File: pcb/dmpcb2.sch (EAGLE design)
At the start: 75 parts, among them IC1 7805DT, IC2 L293D, IC4 LM358D, IC5 LM358D, J7 SJ-3523-SMT-TR, Q1 IRF530, Q2 IRF530

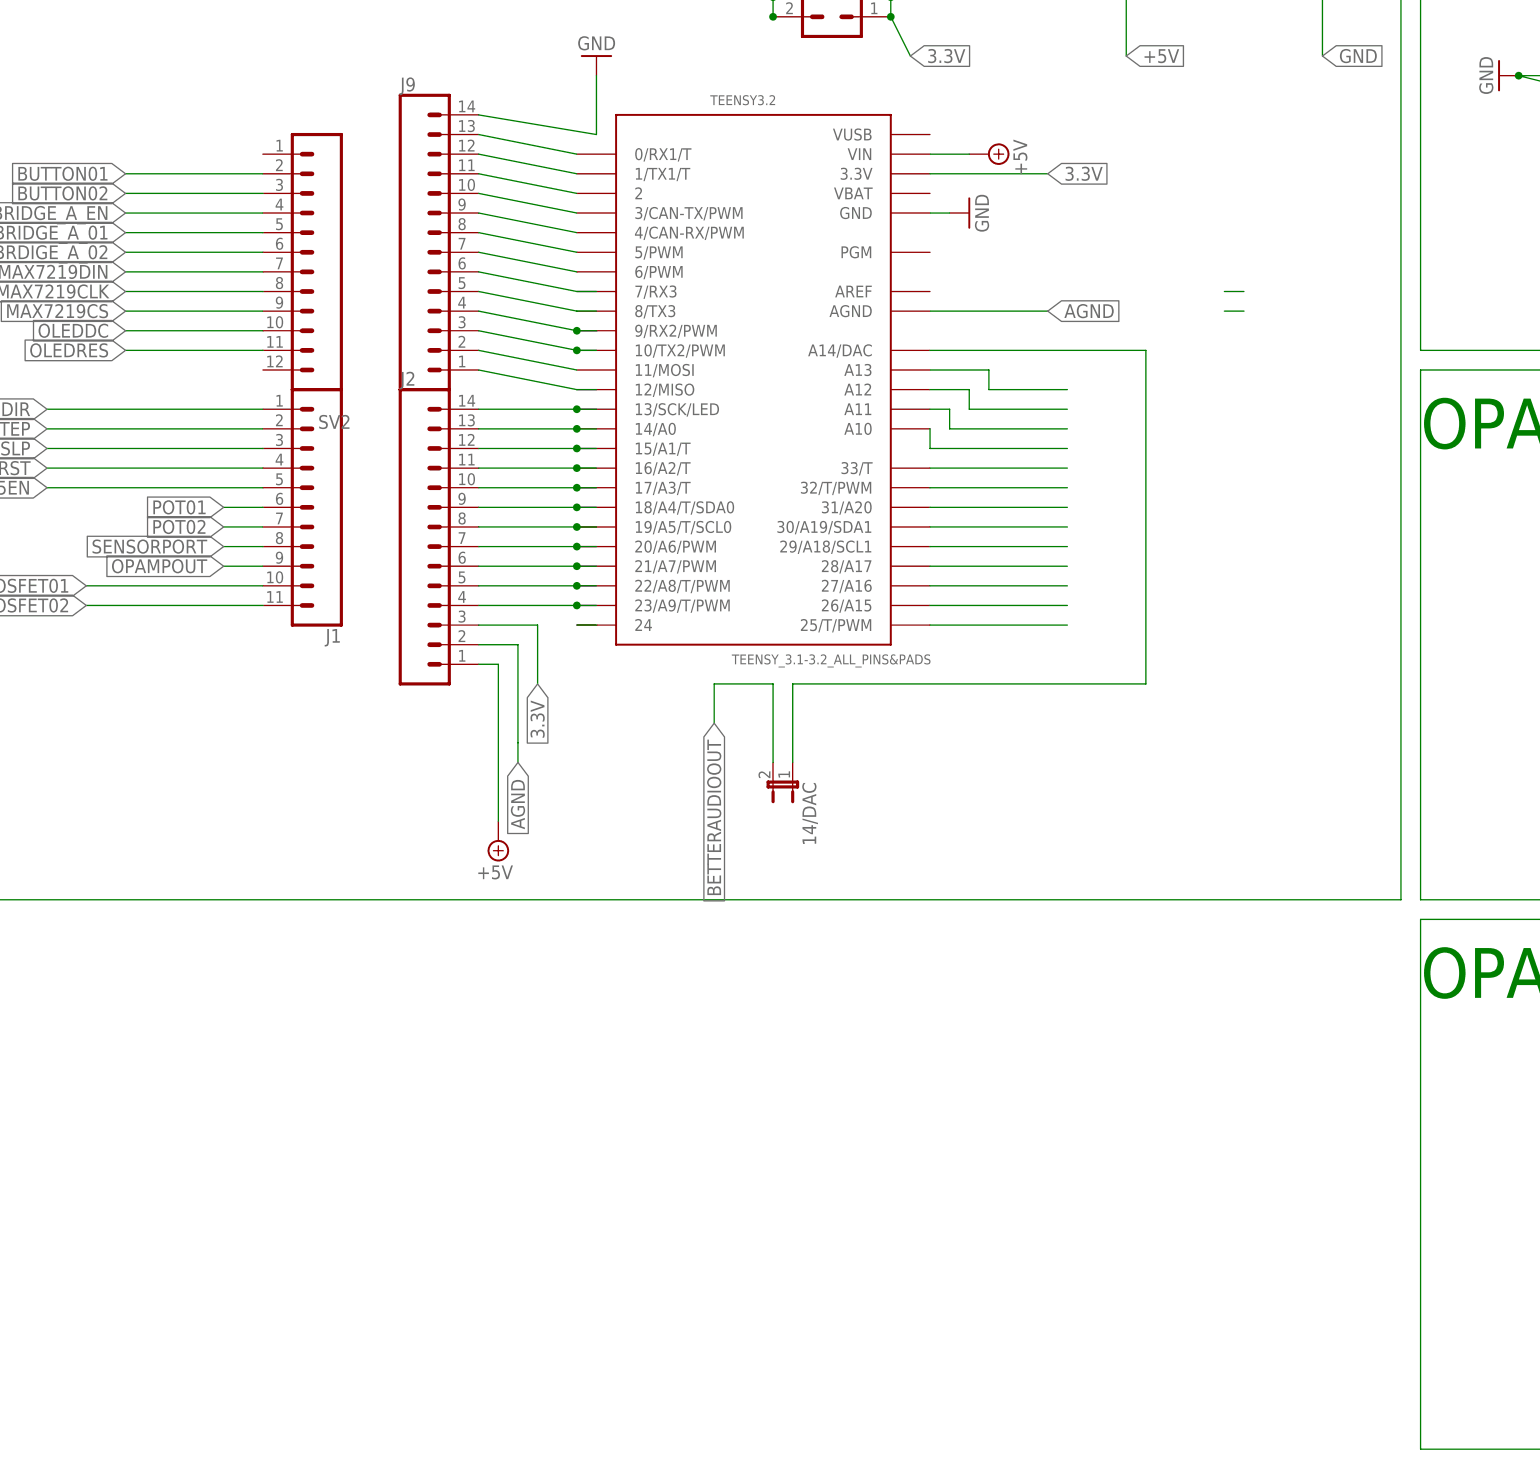
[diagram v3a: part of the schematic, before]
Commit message: added user leds and labeling for opamp
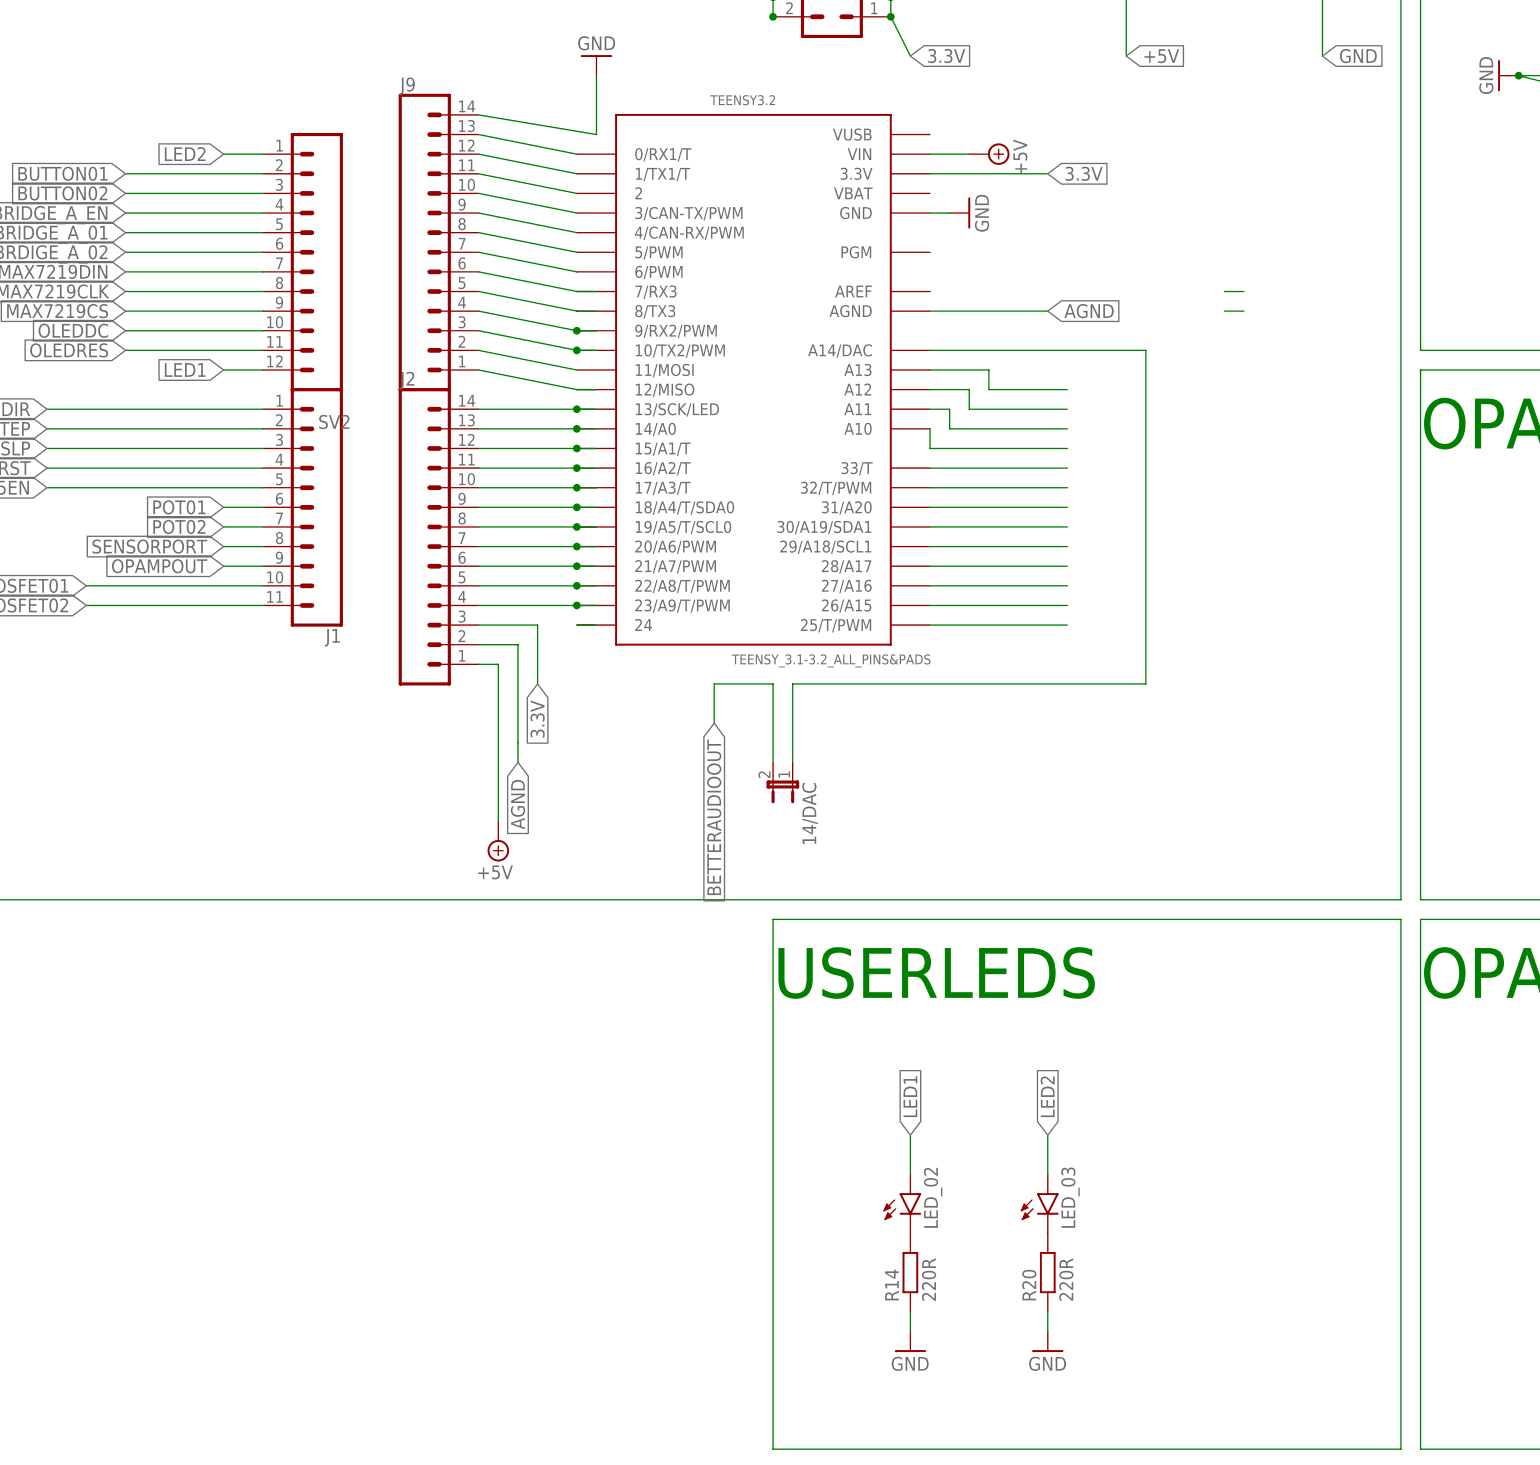
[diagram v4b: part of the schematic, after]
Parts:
- added LED_02, LED_03: (no value), led:LEDSML0805
- added R14, R20: 220R, rcl:R-EU_R0805
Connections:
- new net LED1: LED_02.A, SV2.12
- new net LED2: LED_03.A, SV2.1
- new net N$64: LED_02.C, R14.2
- new net N$76: LED_03.C, R20.2
- net GND: now also R14.1, R20.1
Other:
- note added: "USERLEDS"
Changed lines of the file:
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@@
 </class>
 </classes>
+<groups>
+<schematic_group name="LED"/>
+</groups>
 <parts>
 <part name="GND2" library="supply1" library_urn="urn:adsk.eagle:library:371" deviceset="GND" device=""/>
@@
 <part name="SUPPLY18" library="supply2" library_urn="urn:adsk.eagle:library:372" deviceset="+5V" device=""/>
 <part name="SOCKET_IN1" library="con-lstb" library_urn="urn:adsk.eagle:library:162" deviceset="MA05-1" device="" package3d_urn="urn:adsk.eagle:package:8332/1"/>
+<part name="LED_02" library="led" library_urn="urn:adsk.eagle:library:259" deviceset="LED" device="SML0805" package3d_urn="urn:adsk.eagle:package:15830/1"/>
+<part name="R14" library="rcl" library_urn="urn:adsk.eagle:library:334" deviceset="R-EU_" device="R0805" package3d_urn="urn:adsk.eagle:package:23553/2" value="220R"/>
+<part name="GND31" library="supply1" library_urn="urn:adsk.eagle:library:371" deviceset="GND" device=""/>
+<part name="LED_03" library="led" library_urn="urn:adsk.eagle:library:259" deviceset="LED" device="SML0805" package3d_urn="urn:adsk.eagle:package:15830/1"/>
+<part name="R20" library="rcl" library_urn="urn:adsk.eagle:library:334" deviceset="R-EU_" device="R0805" package3d_urn="urn:adsk.eagle:package:23553/2" value="220R"/>
+<part name="GND32" library="supply1" library_urn="urn:adsk.eagle:library:371" deviceset="GND" device=""/>
 </parts>
 <sheets>
@@
 <text x="238.76" y="-17.78" size="1.778" layer="91">designed by Felix Fisgus</text>
 <text x="152.4" y="-15.24" size="6.4516" layer="91">OPAMP</text>
+<text x="68.58" y="-15.24" size="6.4516" layer="91">USERLEDS</text>
 </plain>
 <instances>
@@
 <attribute name="VALUE" x="54.102" y="196.85" size="1.778" layer="96" rot="R90"/>
 </instance>
-<instance part="LED_01" gate="G$1" x="119.38" y="175.26" smashed="yes">
+<instance part="LED_01" gate="G$1" x="119.38" y="175.26" smashed="yes" grouprefs="LED">
 <attribute name="NAME" x="122.936" y="170.688" size="1.778" layer="95" rot="R90"/>
 <attribute name="VALUE" x="125.095" y="170.688" size="1.778" layer="96" rot="R90"/>
 </instance>
-<instance part="R4" gate="G$1" x="119.38" y="165.1" smashed="yes" rot="R90">
+<instance part="R4" gate="G$1" x="119.38" y="165.1" smashed="yes" rot="R90" grouprefs="LED">
 <attribute name="NAME" x="117.8814" y="161.29" size="1.778" layer="95" rot="R90"/>
 <attribute name="VALUE" x="122.682" y="161.29" size="1.778" layer="96" rot="R90"/>
 </instance>
-<instance part="GND9" gate="1" x="119.38" y="154.94" smashed="yes">
+<instance part="GND9" gate="1" x="119.38" y="154.94" smashed="yes" grouprefs="LED">
 <attribute name="VALUE" x="116.84" y="152.4" size="1.778" layer="96"/>
 </instance>
@@
 <attribute name="VALUE" x="340.614" y="27.94" size="1.778" layer="96" font="vector" rot="R270"/>
 <attribute name="NAME" x="358.648" y="27.94" size="1.778" layer="95" font="vector" rot="R270"/>
+</instance>
+<instance part="LED_02" gate="G$1" x="86.36" y="-40.64" smashed="yes">
+<attribute name="NAME" x="89.916" y="-45.212" size="1.778" layer="95" rot="R90"/>
+<attribute name="VALUE" x="92.075" y="-45.212" size="1.778" layer="96" rot="R90"/>
+</instance>
+<instance part="R14" gate="G$1" x="86.36" y="-50.8" smashed="yes" rot="R90">
+<attribute name="NAME" x="84.8614" y="-54.61" size="1.778" layer="95" rot="R90"/>
+<attribute name="VALUE" x="89.662" y="-54.61" size="1.778" layer="96" rot="R90"/>
+</instance>
+<instance part="GND31" gate="1" x="86.36" y="-60.96" smashed="yes">
+<attribute name="VALUE" x="83.82" y="-63.5" size="1.778" layer="96"/>
+</instance>
+<instance part="LED_03" gate="G$1" x="104.14" y="-40.64" smashed="yes">
+<attribute name="NAME" x="107.696" y="-45.212" size="1.778" layer="95" rot="R90"/>
+<attribute name="VALUE" x="109.855" y="-45.212" size="1.778" layer="96" rot="R90"/>
+</instance>
+<instance part="R20" gate="G$1" x="104.14" y="-50.8" smashed="yes" rot="R90">
+<attribute name="NAME" x="102.6414" y="-54.61" size="1.778" layer="95" rot="R90"/>
+<attribute name="VALUE" x="107.442" y="-54.61" size="1.778" layer="96" rot="R90"/>
+</instance>
+<instance part="GND32" gate="1" x="104.14" y="-60.96" smashed="yes">
+<attribute name="VALUE" x="101.6" y="-63.5" size="1.778" layer="96"/>
 </instance>
 </instances>
@@
 <pinref part="R4" gate="G$1" pin="1"/>
 <pinref part="GND9" gate="1" pin="GND"/>
-<wire x1="119.38" y1="160.02" x2="119.38" y2="157.48" width="0.1524" layer="91"/>
+<wire x1="119.38" y1="160.02" x2="119.38" y2="157.48" width="0.1524" layer="91" grouprefs="LED"/>
 </segment>
 <segment>
@@
 <junction x="370.84" y="0"/>
 </segment>
+<segment>
+<pinref part="R14" gate="G$1" pin="1"/>
+<pinref part="GND31" gate="1" pin="GND"/>
+<wire x1="86.36" y1="-55.88" x2="86.36" y2="-58.42" width="0.1524" layer="91"/>
+</segment>
+<segment>
+<wire x1="104.14" y1="-55.88" x2="104.14" y2="-58.42" width="0.1524" layer="91"/>
+<pinref part="R20" gate="G$1" pin="1"/>
+<pinref part="GND32" gate="1" pin="GND"/>
+</segment>
 </net>
 <net name="V+" class="0">
@@
 <pinref part="LED_01" gate="G$1" pin="A"/>
 <wire x1="119.38" y1="182.88" x2="124.46" y2="182.88" width="0.1524" layer="91"/>
-<wire x1="119.38" y1="177.8" x2="119.38" y2="182.88" width="0.1524" layer="91"/>
+<wire x1="119.38" y1="177.8" x2="119.38" y2="182.88" width="0.1524" layer="91" grouprefs="LED"/>
 <junction x="119.38" y="182.88"/>
 </segment>
@@
 <wire x1="2.54" y1="71.12" x2="-15.24" y2="71.12" width="0.1524" layer="91"/>
 <label x="-15.24" y="71.12" size="1.778" layer="95" rot="R180" xref="yes"/>
+</segment>
+</net>
+<net name="N$21" class="0">
+<segment>
+<wire x1="149.86" y1="-5.08" x2="68.58" y2="-5.08" width="0.1524" layer="91"/>
+<wire x1="68.58" y1="-5.08" x2="68.58" y2="-73.66" width="0.1524" layer="91"/>
+<wire x1="68.58" y1="-73.66" x2="149.86" y2="-73.66" width="0.1524" layer="91"/>
+<wire x1="149.86" y1="-73.66" x2="149.86" y2="-5.08" width="0.1524" layer="91"/>
+</segment>
+</net>
+<net name="LED1" class="0">
+<segment>
+<pinref part="LED_02" gate="G$1" pin="A"/>
+<wire x1="86.36" y1="-38.1" x2="86.36" y2="-33.02" width="0.1524" layer="91"/>
+<label x="86.36" y="-33.02" size="1.778" layer="95" rot="R90" xref="yes"/>
+</segment>
+<segment>
+<pinref part="SV2" gate="G$1" pin="12"/>
+<wire x1="2.54" y1="66.04" x2="-2.54" y2="66.04" width="0.1524" layer="91"/>
+<label x="-2.54" y="66.04" size="1.778" layer="95" rot="R180" xref="yes"/>
+</segment>
+</net>
+<net name="N$64" class="0">
+<segment>
+<pinref part="LED_02" gate="G$1" pin="C"/>
+<pinref part="R14" gate="G$1" pin="2"/>
+</segment>
+</net>
+<net name="LED2" class="0">
+<segment>
+<wire x1="104.14" y1="-38.1" x2="104.14" y2="-33.02" width="0.1524" layer="91"/>
+<pinref part="LED_03" gate="G$1" pin="A"/>
+<label x="104.14" y="-33.02" size="1.778" layer="95" rot="R90" xref="yes"/>
+</segment>
+<segment>
+<pinref part="SV2" gate="G$1" pin="1"/>
+<wire x1="2.54" y1="93.98" x2="-2.54" y2="93.98" width="0.1524" layer="91"/>
+<label x="-2.54" y="93.98" size="1.778" layer="95" rot="R180" xref="yes"/>
+</segment>
+</net>
+<net name="N$76" class="0">
+<segment>
+<pinref part="R20" gate="G$1" pin="2"/>
+<pinref part="LED_03" gate="G$1" pin="C"/>
 </segment>
 </net>
@@
 packages will not be understood (or retained) with this version.
 </note>
+<note version="9.5" severity="warning">
+Since Version 9.5, EAGLE supports persistent groups with
+schematics, and board files. Those persistent groups
+will not be understood (or retained) with this version.
+</note>
 <note version="8.4" severity="warning">
